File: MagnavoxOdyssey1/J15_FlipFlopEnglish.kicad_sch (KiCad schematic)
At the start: 15 parts

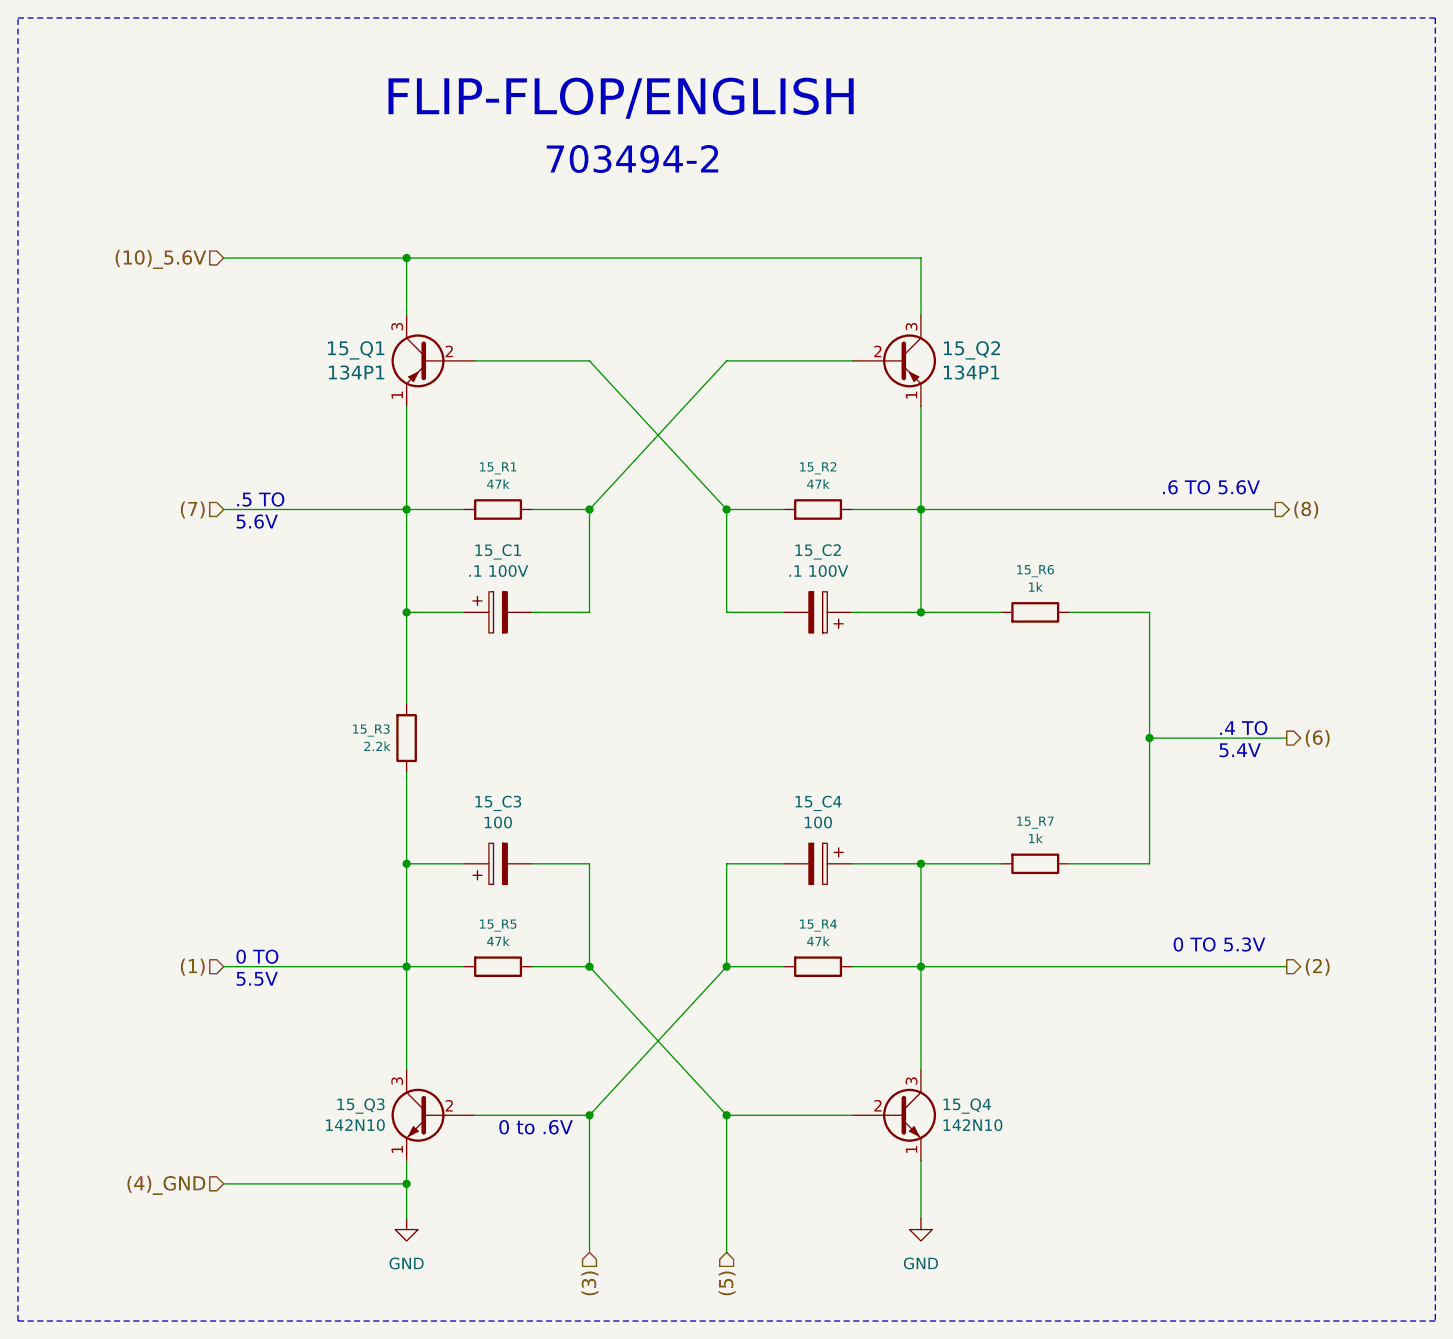
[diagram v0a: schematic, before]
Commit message: update to kicad 9
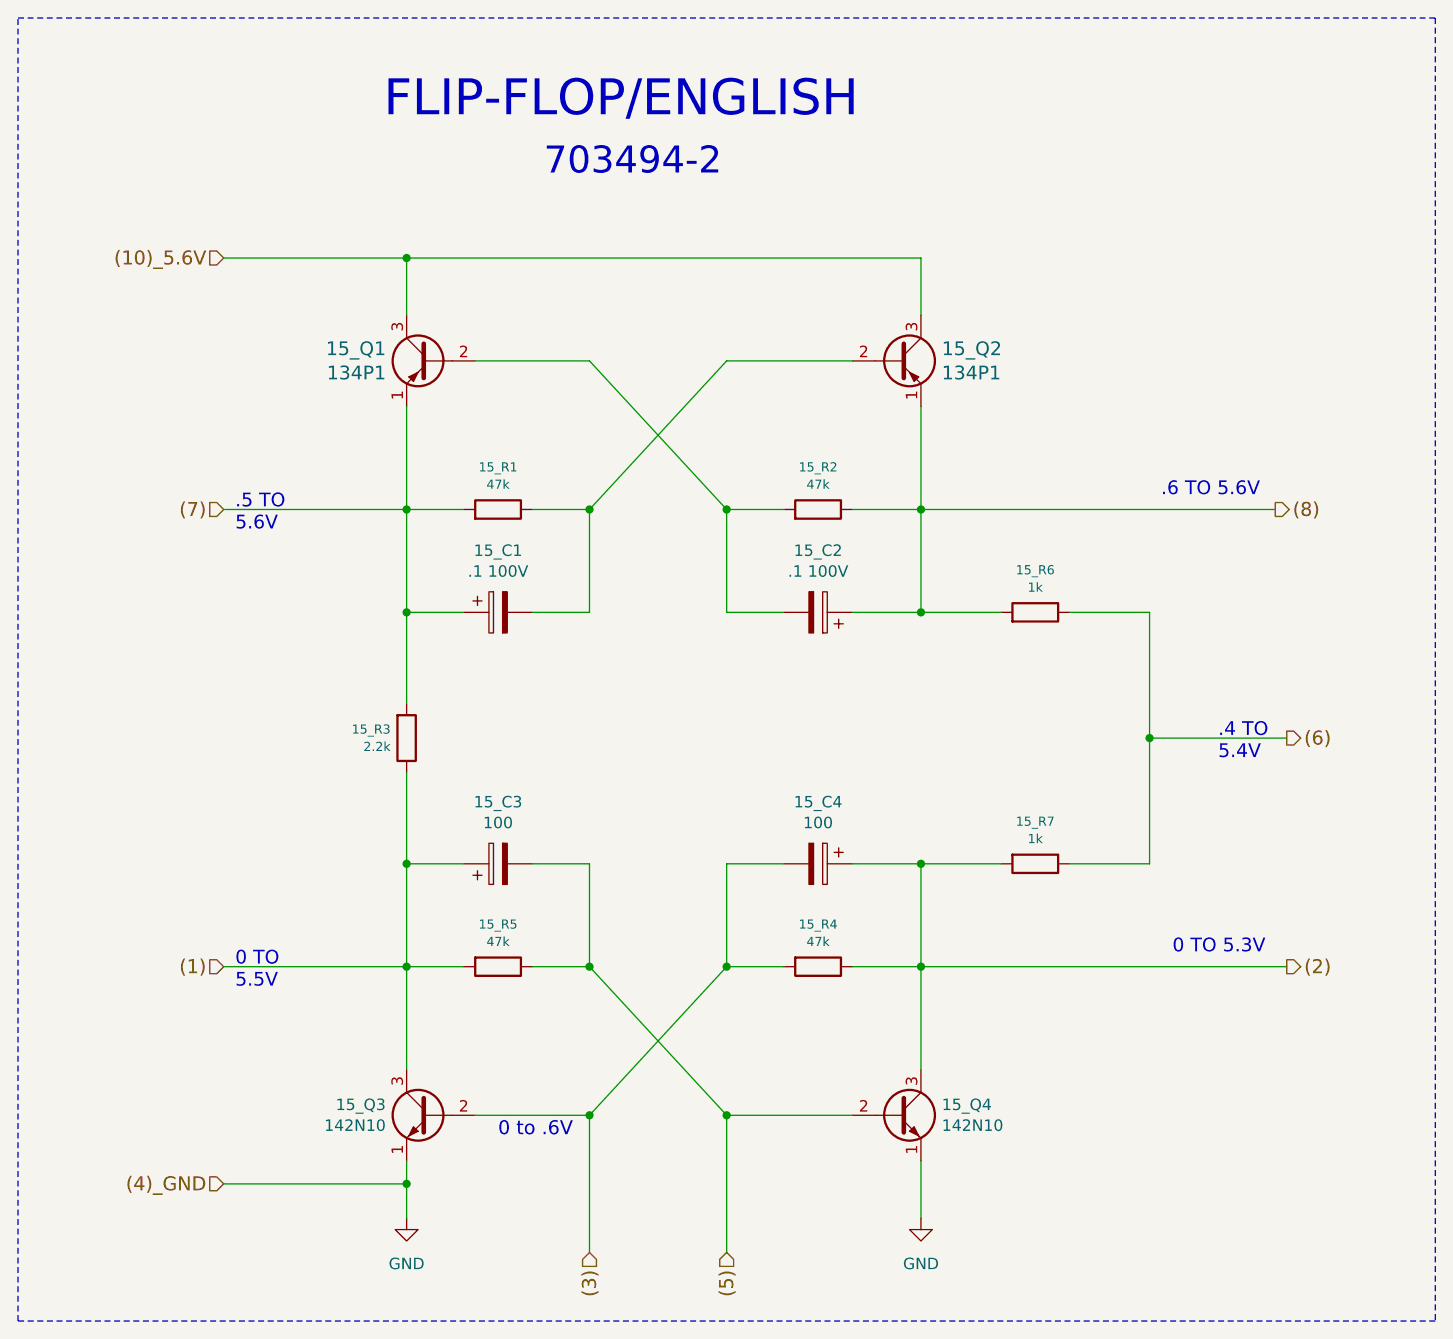
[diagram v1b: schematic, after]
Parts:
- 15_Q1, 15_Q2: symbol Device:Q_PNP_EBC -> Transistor_BJT:Q_PNP_EBC
- 15_Q3, 15_Q4: symbol Device:Q_NPN_EBC -> Transistor_BJT:Q_NPN_EBC
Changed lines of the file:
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@@
 (kicad_sch
-	(version 20231120)
+	(version 20250114)
 	(generator "eeschema")
-	(generator_version "8.0")
+	(generator_version "9.0")
 	(paper "A4")
+	(text "0 to .6V"
+		(exclude_from_sim no)
+		(at 116.84 140.97 0)
+		(effects
+			(font
+				(size 1.5494 1.5494)
+			)
+			(justify left bottom)
+		)
+	)
+	(text "FLIP-FLOP/ENGLISH"
+		(exclude_from_sim no)
+		(at 104.14 27.94 0)
+		(effects
+			(font
+				(size 3.9878 3.9878)
+			)
+			(justify left bottom)
+		)
+	)
+	(text ".6 TO 5.6V"
+		(exclude_from_sim no)
+		(at 190.5 69.85 0)
+		(effects
+			(font
+				(size 1.524 1.524)
+			)
+			(justify left bottom)
+		)
+	)
+	(text ".5 TO\n5.6V"
+		(exclude_from_sim no)
+		(at 87.63 73.66 0)
+		(effects
+			(font
+				(size 1.524 1.524)
+			)
+			(justify left bottom)
+		)
+	)
+	(text "703494-2"
+		(exclude_from_sim no)
+		(at 121.92 34.29 0)
+		(effects
+			(font
+				(size 2.9972 2.9972)
+			)
+			(justify left bottom)
+		)
+	)
+	(text "0 TO 5.3V"
+		(exclude_from_sim no)
+		(at 191.77 120.65 0)
+		(effects
+			(font
+				(size 1.524 1.524)
+			)
+			(justify left bottom)
+		)
+	)
+	(text "0 TO\n5.5V"
+		(exclude_from_sim no)
+		(at 87.63 124.46 0)
+		(effects
+			(font
+				(size 1.524 1.524)
+			)
+			(justify left bottom)
+		)
+	)
+	(text ".4 TO\n5.4V"
+		(exclude_from_sim no)
+		(at 196.85 99.06 0)
+		(effects
+			(font
+				(size 1.524 1.524)
+			)
+			(justify left bottom)
+		)
+	)
 	(junction
 		(at 106.68 110.49)
@@
 			(width 0)
 			(type default)
-		)
-	)
-	(text "0 to .6V"
-		(exclude_from_sim no)
-		(at 116.84 140.97 0)
-		(effects
-			(font
-				(size 1.5494 1.5494)
-			)
-			(justify left bottom)
-		)
-	)
-	(text "FLIP-FLOP/ENGLISH"
-		(exclude_from_sim no)
-		(at 104.14 27.94 0)
-		(effects
-			(font
-				(size 3.9878 3.9878)
-			)
-			(justify left bottom)
-		)
-	)
-	(text ".6 TO 5.6V"
-		(exclude_from_sim no)
-		(at 190.5 69.85 0)
-		(effects
-			(font
-				(size 1.524 1.524)
-			)
-			(justify left bottom)
-		)
-	)
-	(text ".5 TO\n5.6V"
-		(exclude_from_sim no)
-		(at 87.63 73.66 0)
-		(effects
-			(font
-				(size 1.524 1.524)
-			)
-			(justify left bottom)
-		)
-	)
-	(text "703494-2"
-		(exclude_from_sim no)
-		(at 121.92 34.29 0)
-		(effects
-			(font
-				(size 2.9972 2.9972)
-			)
-			(justify left bottom)
-		)
-	)
-	(text "0 TO 5.3V"
-		(exclude_from_sim no)
-		(at 191.77 120.65 0)
-		(effects
-			(font
-				(size 1.524 1.524)
-			)
-			(justify left bottom)
-		)
-	)
-	(text "0 TO\n5.5V"
-		(exclude_from_sim no)
-		(at 87.63 124.46 0)
-		(effects
-			(font
-				(size 1.524 1.524)
-			)
-			(justify left bottom)
-		)
-	)
-	(text ".4 TO\n5.4V"
-		(exclude_from_sim no)
-		(at 196.85 99.06 0)
-		(effects
-			(font
-				(size 1.524 1.524)
-			)
-			(justify left bottom)
 		)
 	)
@@
 	)
 	(symbol
-		(lib_id "Device:Q_NPN_EBC")
+		(lib_id "Transistor_BJT:Q_NPN_EBC")
 		(at 109.22 138.43 0)
 		(mirror y)
@@
 	)
 	(symbol
-		(lib_id "Device:Q_PNP_EBC")
+		(lib_id "Transistor_BJT:Q_PNP_EBC")
 		(at 109.22 54.61 0)
 		(mirror y)
@@
 	)
 	(symbol
-		(lib_id "Device:Q_PNP_EBC")
+		(lib_id "Transistor_BJT:Q_PNP_EBC")
 		(at 161.29 54.61 0)
 		(unit 1)
@@
 	)
 	(symbol
-		(lib_id "Device:Q_NPN_EBC")
+		(lib_id "Transistor_BJT:Q_NPN_EBC")
 		(at 161.29 138.43 0)
 		(unit 1)
